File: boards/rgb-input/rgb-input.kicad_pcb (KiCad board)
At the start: 2 copper layers, 139 x 90 mm, 175 parts, among them J1 Barrel_Jack, J13 I2C, J42 INPUTS, J46 RGB, U1 ESP32-DEVKITC, U13 MCP1502, U2 MCP3208, U3 XL1509-5.0, U5 TLC5947DAP, U6 TLC5947DAP

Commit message: more BOM updates.
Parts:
- C10, C11, C12, C13, C14, C15, C16, C17, C18, C19, C20, C21, C22, C23, C24, C3, C4, C48, C49, C5, C6, C7, C8, C9: value 0.01uf -> 10nF
- D1, D27, D28: footprint Diode_SMD:D_SOD-323_HandSoldering -> Diode_SMD:D_SOD-323
- D32: value PESD5V0L1BA -> SMBJ30CA; footprint Diode_SMD:D_SOD-323_HandSoldering -> Diode_SMD:D_SMB
- F1: value mSMD100 -> mSMD110
- J1: footprint Connector_BarrelJack:BarrelJack_CUI_PJ-063AH_Horizontal -> Connector_BarrelJack:BarrelJack_Horizontal
- moved C2 3.30 mm to (102.7, 128.8)
- moved D32 3.10 mm to (99.1, 130.6)
- moved C1 2.29 mm to (102.7, 132.6), turned to 90 degrees
- moved R39 1.80 mm to (95.3, 132.6)
- moved FB7 1.78 mm to (95.3, 128.8)
- moved J1 1.15 mm to (87.3, 131.7), turned to 0 degrees
- moved F9 1.13 mm to (91.5, 130.1), turned to -90 degrees
- moved D38 1.05 mm to (105.7, 130.3)
- moved L1 0.25 mm to (105.0, 136.7)
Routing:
- net GNDD: track 22.2 -> 12.5 mm, vias 19 -> 20
- net Net-(D32-A2): track 8.14 -> 10.8 mm
- net Net-(F9-Pad1): track 2.47 -> 4.65 mm
- net Net-(C44-Pad2): track 2.03 -> 3.02 mm
- net +24V: track 4.48 -> 3.49 mm
- net Net-(D38-K): track 5.99 -> 6.87 mm
- net Net-(U3-VIN): track 29.8 -> 29.0 mm

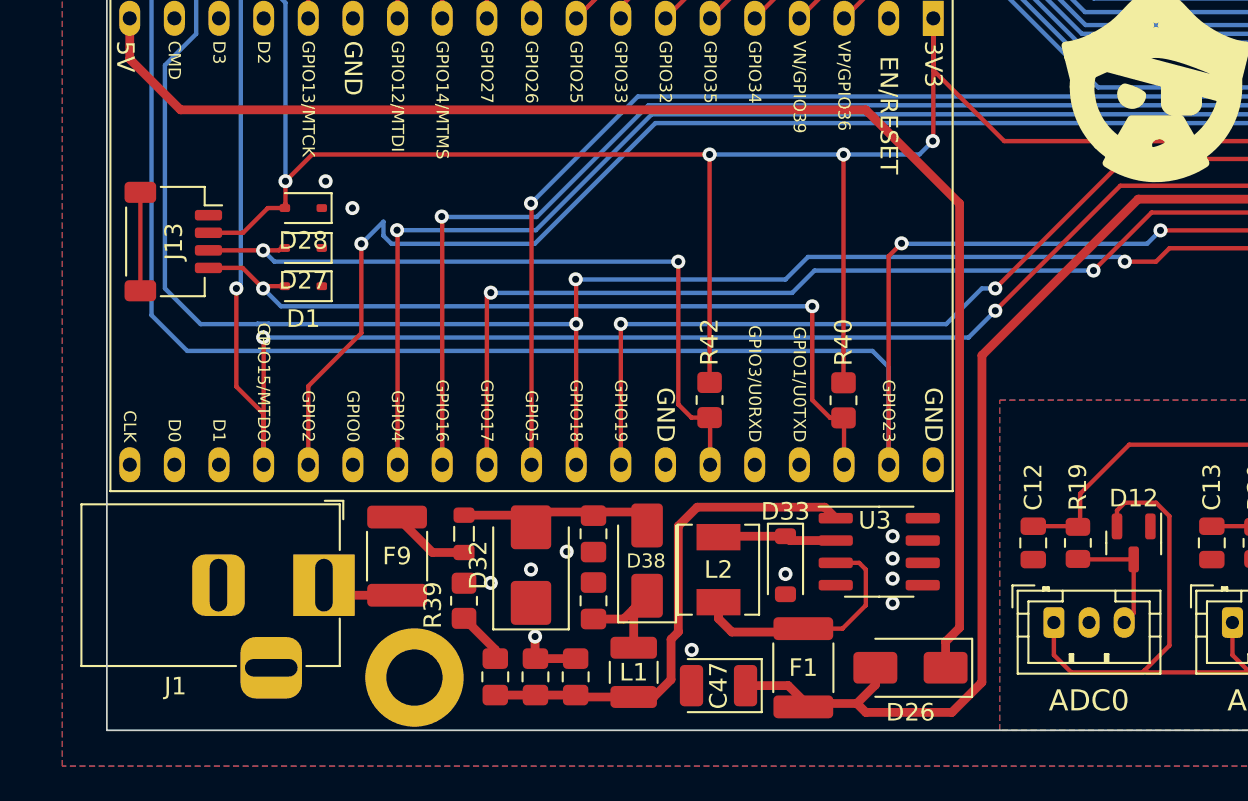
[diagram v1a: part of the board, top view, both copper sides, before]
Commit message: updated inductor footprint
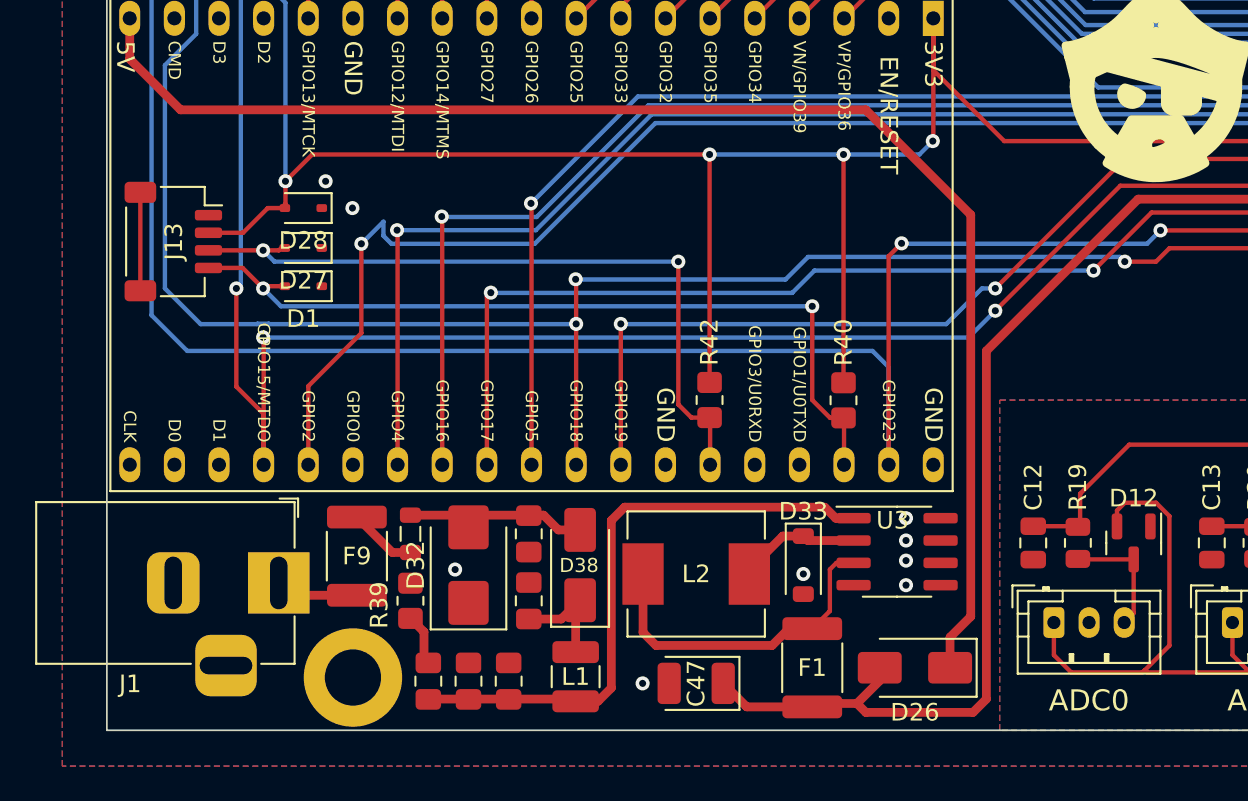
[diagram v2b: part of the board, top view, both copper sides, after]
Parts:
- L2: footprint Inductor_SMD:L_Chilisin_BMRA00040420 -> Inductor_SMD:L_Chilisin_BMRB00060650
- moved D38 3.82 mm to (101.9, 130.6)
- moved C43 3.82 mm to (95.6, 137.2)
- moved C44 3.82 mm to (93.3, 137.2)
- moved C45 3.82 mm to (97.9, 137.2)
- moved C1 3.68 mm to (99.0, 132.6)
- moved C2 3.68 mm to (99.0, 128.8)
- moved D32 3.56 mm to (95.6, 130.6)
- moved H1 3.50 mm to (89.0, 137.0)
- moved L1 3.31 mm to (101.7, 137.0)
- moved FB7 3.05 mm to (92.3, 128.8)
- moved R39 3.05 mm to (92.3, 132.6)
- moved J1 2.57 mm to (84.8, 131.6)
- moved F9 2.29 mm to (89.2, 130.1)
- moved L2 1.29 mm to (108.5, 131.1), turned to 180 degrees
- moved C47 1.28 mm to (108.5, 137.3)
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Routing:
- net Net-(U3-VIN): track 29.0 -> 34.7 mm
- net Net-(U3-FB): track 14.2 -> 19.7 mm
- net GNDD: track 12.5 -> 9.27 mm, vias 20 -> 17
- net +5V: track 333.9 -> 335.8 mm
- net +24V: track 3.49 -> 4.74 mm
- net Net-(D32-A2): track 10.8 -> 10.0 mm
- net Net-(F9-Pad1): track 4.65 -> 3.88 mm

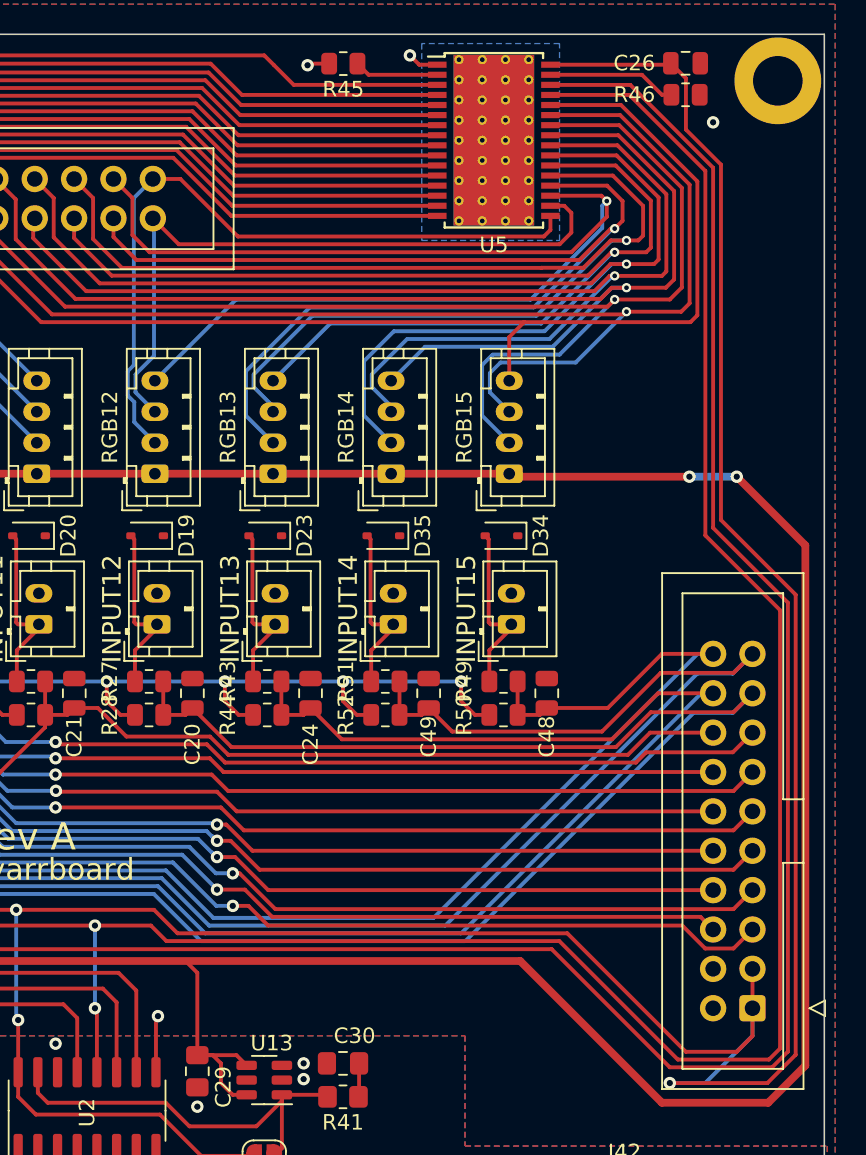
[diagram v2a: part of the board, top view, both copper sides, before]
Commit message: solved the ADC issue and found another minor one
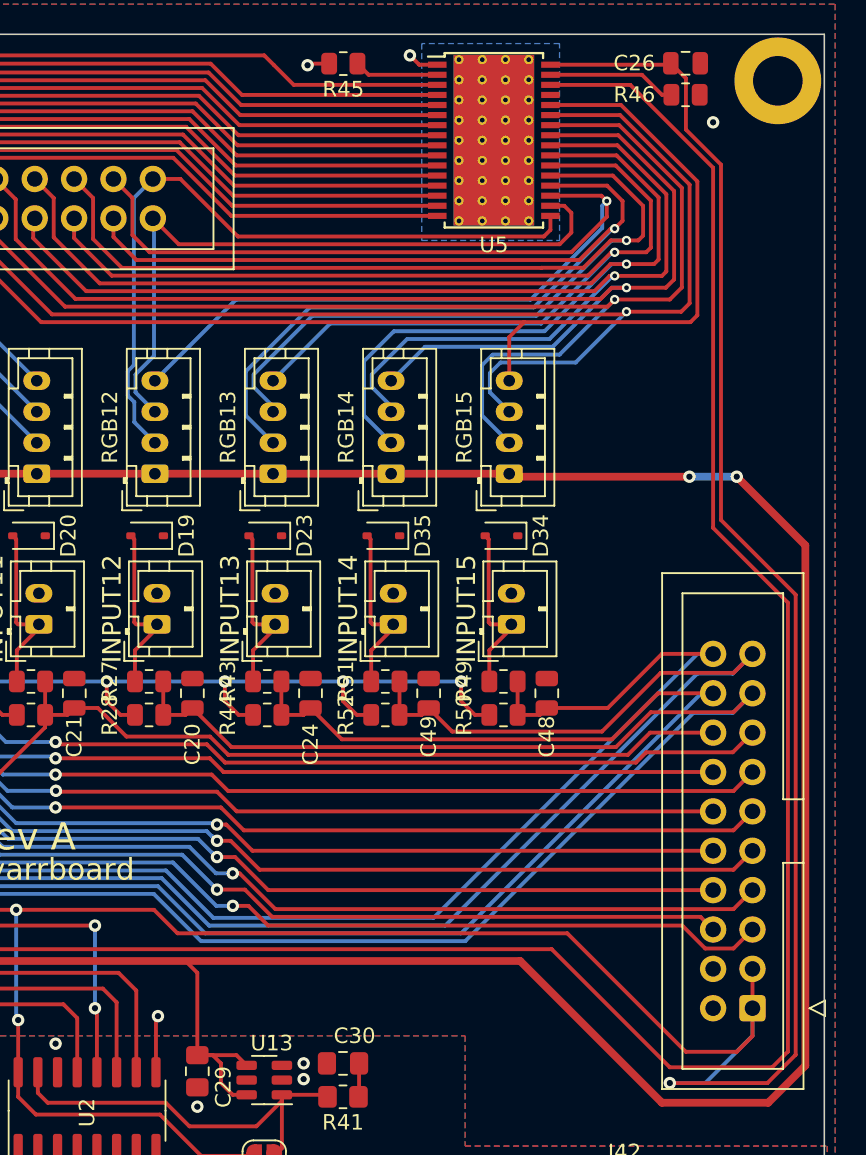
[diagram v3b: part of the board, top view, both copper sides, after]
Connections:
- U5 pad 29: MISO -> /LEDS/LED Driver1/SOUT
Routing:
- net MISO: track 202.8 -> 84.1 mm
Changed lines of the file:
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@@
   (net 137 "unconnected-(H4-Pad1)")
   (net 138 "unconnected-(J13-MountPin-PadMP)")
+  (net 139 "/LEDS/LED Driver1/SOUT")
   (footprint "Connector_JST:JST_PH_B2B-PH-K_1x02_P2.00mm_Vertical" (layer "F.Cu")
     (at 193.81 88.065 90)
@@
       (net 113 "/LEDS/BLUE15") (pinfunction "OUT23") (pintype "output"))
     (pad "29" smd rect (at 3.65 -2.925) (size 1.2 0.4) (layers "F.Cu" "F.Paste" "F.Mask")
-      (net 64 "MISO") (pinfunction "SOUT") (pintype "output"))
+      (net 139 "/LEDS/LED Driver1/SOUT") (pinfunction "SOUT") (pintype "output"))
     (pad "30" smd rect (at 3.65 -3.575) (size 1.2 0.4) (layers "F.Cu" "F.Paste" "F.Mask")
       (net 10 "LED_SS") (pinfunction "XLAT") (pintype "input"))
@@
   (segment (start 101.68694 116.894) (end 84.236516 116.894) (width 0.25) (layer "B.Cu") (net 63))
   (segment (start 84.211016 116.8685) (end 83.568984 116.8685) (width 0.25) (layer "B.Cu") (net 63))
-  (segment (start 211.144 115.424894) (end 211.144 87.148553) (width 0.25) (layer "F.Cu") (net 64))
-  (segment (start 201.422984 53.913) (end 196.332 53.913) (width 0.25) (layer "F.Cu") (net 64))
-  (segment (start 166.948 107.496) (end 170.558894 107.496) (width 0.25) (layer "F.Cu") (net 64))
-  (segment (start 206.326 82.330553) (end 206.326 58.816016) (width 0.25) (layer "F.Cu") (net 64))
   (segment (start 167.075 112.957) (end 166.948 112.83) (width 0.25) (layer "F.Cu") (net 64))
-  (segment (start 196.904 108.496) (end 204.548 116.14) (width 0.25) (layer "F.Cu") (net 64))
   (segment (start 167.075 116.959) (end 167.075 112.957) (width 0.25) (layer "F.Cu") (net 64))
-  (segment (start 171.558894 108.496) (end 196.904 108.496) (width 0.25) (layer "F.Cu") (net 64))
-  (segment (start 211.144 87.148553) (end 206.326 82.330553) (width 0.25) (layer "F.Cu") (net 64))
   (segment (start 125.546 114.862) (end 132.912 107.496) (width 0.25) (layer "F.Cu") (net 64))
-  (segment (start 206.326 58.816016) (end 201.422984 53.913) (width 0.25) (layer "F.Cu") (net 64))
   (segment (start 132.912 107.496) (end 166.948 107.496) (width 0.25) (layer "F.Cu") (net 64))
   (segment (start 104.23944 116.8815) (end 104.23944 124.895) (width 0.25) (layer "F.Cu") (net 64))
-  (segment (start 170.558894 107.496) (end 171.558894 108.496) (width 0.25) (layer "F.Cu") (net 64))
-  (segment (start 204.548 116.14) (end 210.428894 116.14) (width 0.25) (layer "F.Cu") (net 64))
-  (segment (start 210.428894 116.14) (end 211.144 115.424894) (width 0.25) (layer "F.Cu") (net 64))
   (via (at 166.948 112.83) (size 0.8) (drill 0.4) (layers "F.Cu" "B.Cu") (net 64))
   (via (at 166.948 107.496) (size 0.8) (drill 0.4) (layers "F.Cu" "B.Cu") (net 64))

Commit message: new rgb input board coming along very nicely
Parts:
- removed C11, C20, C21, C22, C23, C24, C48, C49: 10nF, Capacitor_SMD:C_0805_2012Metric
- removed C25: 10uF, Capacitor_SMD:C_0805_2012Metric
- removed C29, C30: 100nF, Capacitor_SMD:C_0805_2012Metric_Pad1.18x1.45mm_HandSolder
- removed D10, D19, D20, D21, D22, D23, D34, D35: PESD3V3L1BA, Diode_SMD:D_SOD-323
- removed INPUT10, INPUT11, INPUT12, INPUT13, INPUT14, INPUT15, INPUT8, INPUT9: ~, Connector_JST:JST_PH_B2B-PH-K_1x02_P2.00mm_Vertical
- removed JP1: SolderJumper_2_Open, Jumper:SolderJumper-2_P1.3mm_Open_RoundedPad1.0x1.5mm
- removed R18, R28, R30, R32, R36, R44, R50, R52: 100k, Resistor_SMD:R_0805_2012Metric
- removed R27, R29, R31, R35, R43, R49, R51: 1k, Resistor_SMD:R_0805_2012Metric
- removed R41: 10k, Resistor_SMD:R_0805_2012Metric_Pad1.20x1.40mm_HandSolder
- removed R45, R47: 10k, Resistor_SMD:R_0805_2012Metric
- removed R46: 3.3k, Resistor_SMD:R_0805_2012Metric
- removed RGB10, RGB11, RGB12, RGB13, RGB14, RGB15, RGB8, RGB9: ~, Connector_JST:JST_PH_B4B-PH-K_1x04_P2.00mm_Vertical
- removed U13: MCP1502, Package_TO_SOT_SMD:SOT-23-6
- removed U5: TLC5947DAP, Package_SO:HTSSOP-32-1EP_6.1x11mm_P0.65mm_EP5.2x11mm_Mask4.11x4.36mm_ThermalVias
- C2: value 10nF/50v -> 10nF
- J42: footprint Connector_IDC:IDC-Header_2x10_P2.54mm_Vertical -> Connector_FFC-FPC:Molex_200528-0100_1x10-1MP_P1.00mm_Horizontal
- J46: footprint Connector_IDC:IDC-Header_2x25_P2.54mm_Vertical -> Connector_FFC-FPC:Molex_200528-0300_1x30-1MP_P1.00mm_Horizontal
- R17: value 1k -> 0R; footprint Resistor_SMD:R_0805_2012Metric -> Resistor_SMD:R_0805_2012Metric_Pad1.20x1.40mm_HandSolder
- moved LOGO 102.8 mm to (34.4, 126.0)
- moved U6 95.1 mm to (178.4, 95.9), turned to 90 degrees
- moved J46 94.1 mm to (197.0, 97.0)
- moved H3 84.0 mm to (78.0, 137.0)
- moved R48 78.0 mm to (169.4, 92.4), turned to 180 degrees
- moved U2 69.3 mm to (98.5, 133.0), turned to -90 degrees
- moved R38 62.7 mm to (92.5, 123.3), turned to 90 degrees
- moved D7 60.1 mm to (172.0, 106.4)
- moved INPUT7 60.1 mm to (187.9, 112.2)
- moved R7 60.1 mm to (156.9, 115.8)
- moved R8 60.1 mm to (156.9, 118.0)
- moved C3 60.1 mm to (136.8, 116.3)
- moved C7 60.1 mm to (167.3, 116.6)
- moved C8 60.1 mm to (174.9, 116.6)
- moved C9 60.1 mm to (182.5, 116.6)
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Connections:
- ADC0 pad 1: REF_3V3 -> +3.3V
- ADC0 pad 2: GNDA -> Net-(ADC0-Pin_2)
- ADC0 pad 3: Net-(ADC0-Pin_3) -> GNDA
- ADC1 pad 1: REF_3V3 -> +3.3V
- ADC1 pad 2: GNDA -> Net-(ADC1-Pin_2)
- ADC1 pad 3: Net-(ADC1-Pin_3) -> GNDA
- ADC2 pad 1: REF_3V3 -> +3.3V
- ADC2 pad 2: GNDA -> Net-(ADC2-Pin_2)
- ADC2 pad 3: Net-(ADC2-Pin_3) -> GNDA
- ADC3 pad 1: REF_3V3 -> +3.3V
- ADC3 pad 2: GNDA -> Net-(ADC3-Pin_2)
- ADC3 pad 3: Net-(ADC3-Pin_3) -> GNDA
- ADC4 pad 1: REF_3V3 -> +3.3V
- ADC4 pad 2: GNDA -> Net-(ADC4-Pin_2)
- ADC4 pad 3: Net-(ADC4-Pin_3) -> GNDA
- ADC5 pad 1: REF_3V3 -> +3.3V
- ADC5 pad 2: GNDA -> Net-(ADC5-Pin_2)
- ADC5 pad 3: Net-(ADC5-Pin_3) -> GNDA
- ADC6 pad 1: REF_3V3 -> +3.3V
- ADC6 pad 2: GNDA -> Net-(ADC6-Pin_2)
- ADC6 pad 3: Net-(ADC6-Pin_3) -> GNDA
- ADC7 pad 1: REF_3V3 -> +3.3V
- ADC7 pad 2: GNDA -> Net-(ADC7-Pin_2)
- ADC7 pad 3: Net-(ADC7-Pin_3) -> GNDA
- D11 pad 2: REF_3V3 -> +3.3V
- D11 pad 3: Net-(ADC1-Pin_3) -> Net-(ADC1-Pin_2)
- D12 pad 2: REF_3V3 -> +3.3V
- D12 pad 3: Net-(ADC0-Pin_3) -> Net-(ADC0-Pin_2)
- D13 pad 2: REF_3V3 -> +3.3V
- D13 pad 3: Net-(ADC2-Pin_3) -> Net-(ADC2-Pin_2)
- D14 pad 2: REF_3V3 -> +3.3V
- D14 pad 3: Net-(ADC3-Pin_3) -> Net-(ADC3-Pin_2)
- D15 pad 2: REF_3V3 -> +3.3V
- D15 pad 3: Net-(ADC4-Pin_3) -> Net-(ADC4-Pin_2)
- D16 pad 2: REF_3V3 -> +3.3V
- D16 pad 3: Net-(ADC5-Pin_3) -> Net-(ADC5-Pin_2)
- D17 pad 2: REF_3V3 -> +3.3V
- D17 pad 3: Net-(ADC6-Pin_3) -> Net-(ADC6-Pin_2)
- D18 pad 2: REF_3V3 -> +3.3V
- D18 pad 3: Net-(ADC7-Pin_3) -> Net-(ADC7-Pin_2)
- J42 pad 10: /INPUT5 -> /INPUT7
- J42 pad 3: +3.3V -> /INPUT0
- J42 pad 4: GNDD -> /INPUT1
- J42 pad 5: /INPUT0 -> /INPUT2
- J42 pad 6: /INPUT1 -> /INPUT3
- J42 pad 7: /INPUT2 -> /INPUT4
- J42 pad 8: /INPUT3 -> /INPUT5
- J42 pad 9: /INPUT4 -> /INPUT6
- J46 pad 10: /LEDS/GREEN1 -> /LEDS/RED1
- J46 pad 11: /LEDS/RED1 -> /LEDS/GREEN1
- J46 pad 12: /LEDS/BLUE0 -> /LEDS/BLUE1
- J46 pad 13: /LEDS/GREEN0 -> /LEDS/RED2
- J46 pad 14: /LEDS/RED0 -> /LEDS/GREEN2
- J46 pad 15: /LEDS/RED4 -> /LEDS/BLUE2
- J46 pad 16: /LEDS/GREEN4 -> /LEDS/RED3
- J46 pad 17: /LEDS/BLUE4 -> /LEDS/GREEN3
- J46 pad 18: /LEDS/RED5 -> /LEDS/BLUE3
- J46 pad 19: /LEDS/GREEN5 -> /LEDS/RED4
- J46 pad 2: GNDD -> +5V
- J46 pad 20: /LEDS/BLUE5 -> /LEDS/GREEN4
- J46 pad 21: /LEDS/RED6 -> /LEDS/BLUE4
- J46 pad 22: /LEDS/GREEN6 -> /LEDS/RED5
- J46 pad 23: /LEDS/BLUE6 -> /LEDS/GREEN5
- J46 pad 24: /LEDS/RED7 -> /LEDS/BLUE5
- J46 pad 25: /LEDS/GREEN7 -> /LEDS/RED6
- J46 pad 26: /LEDS/BLUE7 -> /LEDS/GREEN6
- J46 pad 27: /LEDS/RED8 -> /LEDS/BLUE6
- J46 pad 28: /LEDS/GREEN8 -> /LEDS/RED7
- J46 pad 29: /LEDS/BLUE8 -> /LEDS/GREEN7
- J46 pad 3: /LEDS/BLUE3 -> +5V
- J46 pad 30: /LEDS/RED9 -> /LEDS/BLUE7
- J46 pad 4: /LEDS/GREEN3 -> GNDD
- J46 pad 5: /LEDS/RED3 -> GNDD
- J46 pad 6: /LEDS/BLUE2 -> GNDD
- J46 pad 7: /LEDS/GREEN2 -> /LEDS/RED0
- J46 pad 8: /LEDS/RED2 -> /LEDS/GREEN0
- J46 pad 9: /LEDS/BLUE1 -> /LEDS/BLUE0
- R17 pad 1: Net-(D10-A2) -> Net-(U1-GPIO12)
- R17 pad 2: /INPUT8 -> LED_MISO
- R19 pad 1: Net-(ADC0-Pin_3) -> Net-(ADC0-Pin_2)
- R20 pad 1: Net-(ADC1-Pin_3) -> Net-(ADC1-Pin_2)
- R21 pad 1: Net-(ADC2-Pin_3) -> Net-(ADC2-Pin_2)
- R22 pad 1: Net-(ADC3-Pin_3) -> Net-(ADC3-Pin_2)
- R23 pad 1: Net-(ADC4-Pin_3) -> Net-(ADC4-Pin_2)
- R24 pad 1: Net-(ADC5-Pin_3) -> Net-(ADC5-Pin_2)
- R25 pad 1: Net-(ADC6-Pin_3) -> Net-(ADC6-Pin_2)
- R26 pad 1: Net-(ADC7-Pin_3) -> Net-(ADC7-Pin_2)
- U1 pad 10: /INPUT4 -> /INPUT0
- U1 pad 11: /INPUT3 -> LED_SS
- U1 pad 12: /INPUT2 -> LED_SCK
- U1 pad 13: /INPUT1 -> Net-(U1-GPIO12)
- U1 pad 15: /INPUT0 -> LED_MOSI
- U1 pad 23: LED_SS -> unconnected-(U1-GPIO15-Pad23)
- U1 pad 24: /INPUT12 -> unconnected-(U1-GPIO2-Pad24)
- U1 pad 26: /INPUT13 -> LED_BLANK
- U1 pad 27: /INPUT14 -> unconnected-(U1-GPIO16-Pad27)
- U1 pad 29: /INPUT15 -> unconnected-(U1-GPIO5-Pad29)
- U1 pad 3: /INPUT11 -> /INPUT7
- U1 pad 30: SCK -> ADC_SCK
- U1 pad 31: MISO -> ADC_MISO
- U1 pad 33: SDA -> SCA
- U1 pad 37: MOSI -> ADC_MOSI
- U1 pad 4: /INPUT10 -> /INPUT6
- U1 pad 5: /INPUT9 -> /INPUT5
- U1 pad 6: /INPUT8 -> /INPUT4
- U1 pad 7: /INPUT7 -> /INPUT3
- U1 pad 8: /INPUT6 -> /INPUT2
- U1 pad 9: /INPUT5 -> /INPUT1
- U2 pad 15: REF_3V3 -> +3.3V
- U6 pad 2: /LEDS/LED Driver/BLANK -> LED_BLANK
- U6 pad 29: /LEDS/LED Driver/SOUT -> LED_MISO
- U6 pad 3: SCK -> LED_SCK
- U6 pad 4: MOSI -> LED_MOSI
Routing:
- net +3.3V: track 534.3 -> 0.00 mm, vias 24 -> 0
- net +5V: track 335.8 -> 0.00 mm, vias 3 -> 0
- net LED_SS: track 322.5 -> 0.00 mm, vias 4 -> 0
- net SCK: track 322.3 -> 0.00 mm, vias 4 -> 0
- net REF_3V3: track 269.8 -> 0.00 mm
- net MOSI: track 222.3 -> 0.00 mm, vias 3 -> 0
- net /INPUT12: track 188.8 -> 0.00 mm, vias 1 -> 0
- net /INPUT13: track 171.3 -> 0.00 mm, vias 1 -> 0
- net /INPUT14: track 168.4 -> 0.00 mm, vias 1 -> 0
- net /INPUT15: track 149.8 -> 0.00 mm, vias 1 -> 0
- net /INPUT8: track 109.2 -> 0.00 mm, vias 2 -> 0
- net /INPUT9: track 103.3 -> 0.00 mm, vias 2 -> 0
- net /INPUT10: track 102.7 -> 0.00 mm, vias 2 -> 0
- net /INPUT7: track 109.5 -> 7.16 mm, vias 2 -> 0
- net /INPUT6: track 115.0 -> 15.2 mm, vias 2 -> 0
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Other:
- board size 139 x 90 mm -> 127 x 68 mm

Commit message: new rgb input board is starting to look very nice.
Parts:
- J42: footprint Connector_FFC-FPC:Molex_200528-0100_1x10-1MP_P1.00mm_Horizontal -> Connector_FFC-FPC:TE_1-84952-0_1x10-1MP_P1.0mm_Horizontal
- J46: footprint Connector_FFC-FPC:Molex_200528-0300_1x30-1MP_P1.00mm_Horizontal -> Connector_FFC-FPC:TE_3-84952-0_1x30-1MP_P1.0mm_Horizontal
- moved LOGO 102.5 mm to (129.9, 88.9)
- moved D2 21.2 mm to (133.9, 106.2)
- moved H1 18.4 mm to (78.0, 72.0)
- moved R38 10.4 mm to (86.9, 132.1), turned to 180 degrees
- moved U3 3.89 mm to (126.3, 73.5)
- moved U2 3.71 mm to (94.9, 132.2)
- moved D11 3.67 mm to (120.5, 130.3), turned to 90 degrees
- moved D12 3.67 mm to (110.3, 130.3), turned to 90 degrees
- moved D13 3.67 mm to (130.6, 130.3), turned to 90 degrees
- moved D14 3.67 mm to (140.8, 130.3), turned to 90 degrees
- moved D15 3.67 mm to (150.9, 130.3), turned to 90 degrees
- moved D16 3.67 mm to (161.1, 130.3), turned to 90 degrees
- moved D17 3.67 mm to (171.3, 130.3), turned to 90 degrees
- moved D18 3.67 mm to (181.4, 130.3), turned to 90 degrees
- moved ADC1 3.66 mm to (115.9, 134.9)
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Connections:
- J13 pad MP: unconnected-(J13-MountPin-PadMP) -> GNDD
- U1 pad 33: SCA -> SDA
- U2 pad 11: MOSI -> ADC_MOSI
- U2 pad 12: MISO -> ADC_MISO
- U2 pad 13: SCK -> ADC_SCK
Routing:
- net +3.3V: track 0.00 -> 417.1 mm, vias 0 -> 11
- net +5V: track 0.00 -> 122.9 mm
- net LED_MOSI: track 0.00 -> 100.1 mm
- net LED_MISO: track 0.00 -> 99.3 mm, vias 0 -> 2
- net /INPUT7: track 7.16 -> 103.6 mm, vias 0 -> 3
- net LED_SS: track 0.00 -> 95.3 mm
- net LED_BLANK: track 0.00 -> 95.2 mm, vias 0 -> 1
- net /INPUT6: track 15.2 -> 107.6 mm, vias 0 -> 1
- net LED_SCK: track 0.00 -> 89.7 mm
- net /INPUT5: track 23.2 -> 111.6 mm, vias 0 -> 1
- net /INPUT4: track 31.3 -> 113.4 mm, vias 0 -> 2
- net /INPUT3: track 39.3 -> 116.4 mm, vias 0 -> 2
- net /INPUT2: track 47.3 -> 120.9 mm, vias 0 -> 2
- net /INPUT1: track 55.4 -> 122.6 mm, vias 0 -> 2
- net /INPUT0: track 63.5 -> 123.9 mm, vias 0 -> 2
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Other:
- board size 127 x 68 mm -> 127 x 71 mm
- board text added: "RGB I/O Board Rev B"
- board text removed: "RGB I/O Board Rev A"

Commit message: passing ERC and DRC
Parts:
- moved C1 0.67 mm to (103.1, 77.0)
- moved C2 0.41 mm to (103.1, 72.4)
- moved FB7 0.41 mm to (95.8, 72.4)
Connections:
- J42 pad MP: (no net) -> GNDD
- J46 pad MP: (no net) -> GNDD
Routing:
- net Net-(D32-A2): track 12.2 -> 11.6 mm
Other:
- board text added: "12-24V INPUT"
- board text added: "INPUTS FFC"
- board text added: "RGB LEDS FFC"

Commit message: reannotated and did some more cleanup.  almost ready
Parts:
- renumbered C4 to C1, C12 to C10, C44 to C11, C2 to C12, C1 to C13, C43 to C14, C45 to C15, C47 to C16, C14 to C17, C15 to C18, C16 to C19, C6 to C2, C17 to C20, C18 to C21, C19 to C22, C26 to C23, C5 to C3, C3 to C4, C7 to C5, C8 to C6, C9 to C7, C10 to C8, C13 to C9, D8 to D10, D9 to D11, D11 to D12, D12 to D13, D38 to D14, D26 to D15, D32 to D16, D33 to D17, D13 to D18, D14 to D19, D27 to D2, D15 to D20, D16 to D21, D17 to D22, D18 to D23, D28 to D3, D3 to D4, D4 to D6, D2 to D7, D6 to D8, D7 to D9, F9 to F1, F1 to F2, FB7 to FB1, J42 to J1, J13 to J2, J1 to J3, J46 to J4, R17 to R1, R2 to R10, R1 to R11, R10 to R12, R9 to R13, R12 to R14, R11 to R15, R14 to R16, R13 to R17, R16 to R18, R15 to R19, R40 to R2, R19 to R21, R39 to R22, R38 to R23, R21 to R24, R22 to R25, R23 to R26, R24 to R27, R25 to R28, R26 to R29, R42 to R3, R48 to R30, R3 to R5, R8 to R6, R6 to R8, R5 to R9, U6 to U4
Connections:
- H1 pad 1: unconnected-(H1-Pad1) -> GNDD
- H2 pad 1: unconnected-(H2-Pad1) -> GNDD
- H3 pad 1: unconnected-(H3-Pad1) -> GNDD
- H4 pad 1: unconnected-(H4-Pad1) -> GNDD
- J3 pad 3: (no net) -> unconnected-(J3-Pad3)
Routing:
- net +3.3V: track 417.1 -> 395.8 mm
- net ADC_SCK: track 49.8 -> 48.1 mm
- net ADC_MISO: track 48.6 -> 47.1 mm
- net ADC_SS: track 39.2 -> 37.8 mm
- net ADC_MOSI: track 57.3 -> 56.3 mm
- net GNDD: track 16.3 -> 15.5 mm, vias 19 -> 21
- net GNDA: vias 21 -> 22
